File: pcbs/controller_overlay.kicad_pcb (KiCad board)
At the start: 2 copper layers, 19.7 x 60.1 mm, 2 parts

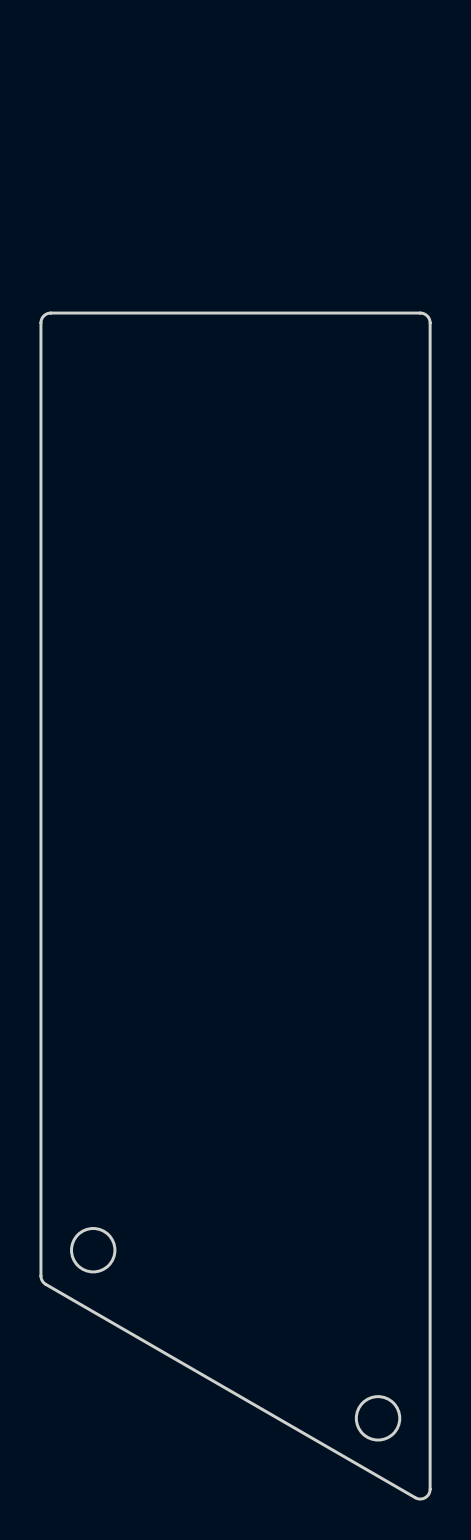
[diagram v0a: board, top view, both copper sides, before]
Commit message: feat: PCB holes alignment
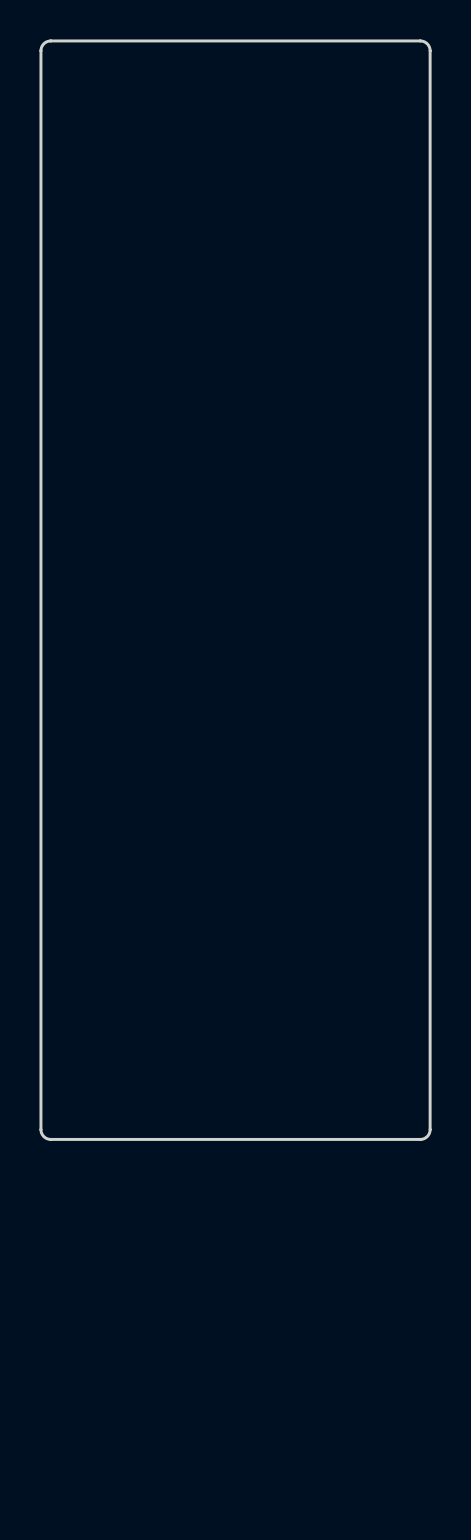
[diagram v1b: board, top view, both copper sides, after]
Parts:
- removed MH1, MH2: , ceoloide:mounting_hole_npth
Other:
- board size 19.7 x 60.1 mm -> 19.7 x 55.7 mm
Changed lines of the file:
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@@
   (title_block
     (title "controller_overlay")
-    (date "2024-11-14")
-    (rev "0.2")
-    (company "ceoloide")
+    (date "2025-02-11")
+    (rev "0.1")
+    (company "fcoury (adapted from corney-island)")
   )
   (layers
@@
   )
   (net 0 "")
-  (footprint "ceoloide:mounting_hole_npth"
-    (layer "F.Cu")
-    (at 207.762 100.476 0)
-    (property "Reference" "MH1"
-      (at 0 2.55 0)
-      (layer "F.SilkS")
-      hide
-      (effects (font (size 1 1) (thickness 0.15)))
-    )
-    (pad "" np_thru_hole circle
-      (at 0 0 0)
-      (size 2.2 2.2)
-      (drill 2.2)
-      (layers "*.Cu" "*.Mask")
-    )
-  )
-  (footprint "ceoloide:mounting_hole_npth"
-    (layer "F.Cu")
-    (at 222.194 108.995 0)
-    (property "Reference" "MH2"
-      (at 0 2.55 0)
-      (layer "F.SilkS")
-      hide
-      (effects (font (size 1 1) (thickness 0.15)))
-    )
-    (pad "" np_thru_hole circle
-      (at 0 0 0)
-      (size 2.2 2.2)
-      (drill 2.2)
-      (layers "*.Cu" "*.Mask")
-    )
-  )
-  (gr_line (start 205.113 101.77697755907997) (end 205.113 53.49) (layer Edge.Cuts) (stroke (width 0.15) (type default)))
-(gr_line (start 205.613 52.99) (end 224.333 52.99) (layer Edge.Cuts) (stroke (width 0.15) (type default)))
-(gr_line (start 224.833 53.49) (end 224.833 112.58497459811554) (layer Edge.Cuts) (stroke (width 0.15) (type default)))
-(gr_line (start 224.08299999999997 113.01798729811554) (end 205.36299999999997 102.20999025907994) (layer Edge.Cuts) (stroke (width 0.15) (type default)))
-(gr_arc (start 205.613 52.99) (mid 205.2594466 53.1364466) (end 205.113 53.49) (layer Edge.Cuts) (stroke (width 0.15) (type default)))
-(gr_arc (start 224.833 53.49) (mid 224.6865534 53.1364466) (end 224.333 52.99) (layer Edge.Cuts) (stroke (width 0.15) (type default)))
-(gr_arc (start 224.083 113.01798729811554) (mid 224.583 113.01798729811554) (end 224.833 112.58497459811554) (layer Edge.Cuts) (stroke (width 0.15) (type default)))
-(gr_arc (start 205.113 101.77697755907997) (mid 205.1799873 102.02697755907997) (end 205.363 102.20999025907997) (layer Edge.Cuts) (stroke (width 0.15) (type default)))
-(gr_circle (center 207.762 100.476) (end 208.862 100.476) (layer Edge.Cuts) (stroke (width 0.15) (type default)) (fill none))
-(gr_circle (center 222.194 108.995) (end 223.29399999999998 108.995) (layer Edge.Cuts) (stroke (width 0.15) (type default)) (fill none))
+  (gr_line (start 205.113 94.3635) (end 205.113 39.7025) (layer Edge.Cuts) (stroke (width 0.15) (type default)))
+(gr_line (start 205.613 39.2025) (end 224.333 39.2025) (layer Edge.Cuts) (stroke (width 0.15) (type default)))
+(gr_line (start 224.833 39.7025) (end 224.833 94.3635) (layer Edge.Cuts) (stroke (width 0.15) (type default)))
+(gr_line (start 224.333 94.8635) (end 205.613 94.8635) (layer Edge.Cuts) (stroke (width 0.15) (type default)))
+(gr_arc (start 205.613 39.2025) (mid 205.2594466 39.3489466) (end 205.113 39.7025) (layer Edge.Cuts) (stroke (width 0.15) (type default)))
+(gr_arc (start 224.833 39.7025) (mid 224.6865534 39.3489466) (end 224.333 39.2025) (layer Edge.Cuts) (stroke (width 0.15) (type default)))
+(gr_arc (start 224.333 94.8635) (mid 224.6865534 94.7170534) (end 224.833 94.3635) (layer Edge.Cuts) (stroke (width 0.15) (type default)))
+(gr_arc (start 205.113 94.3635) (mid 205.2594466 94.7170534) (end 205.613 94.8635) (layer Edge.Cuts) (stroke (width 0.15) (type default)))
 )
